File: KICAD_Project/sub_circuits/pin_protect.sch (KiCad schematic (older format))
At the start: 84 parts

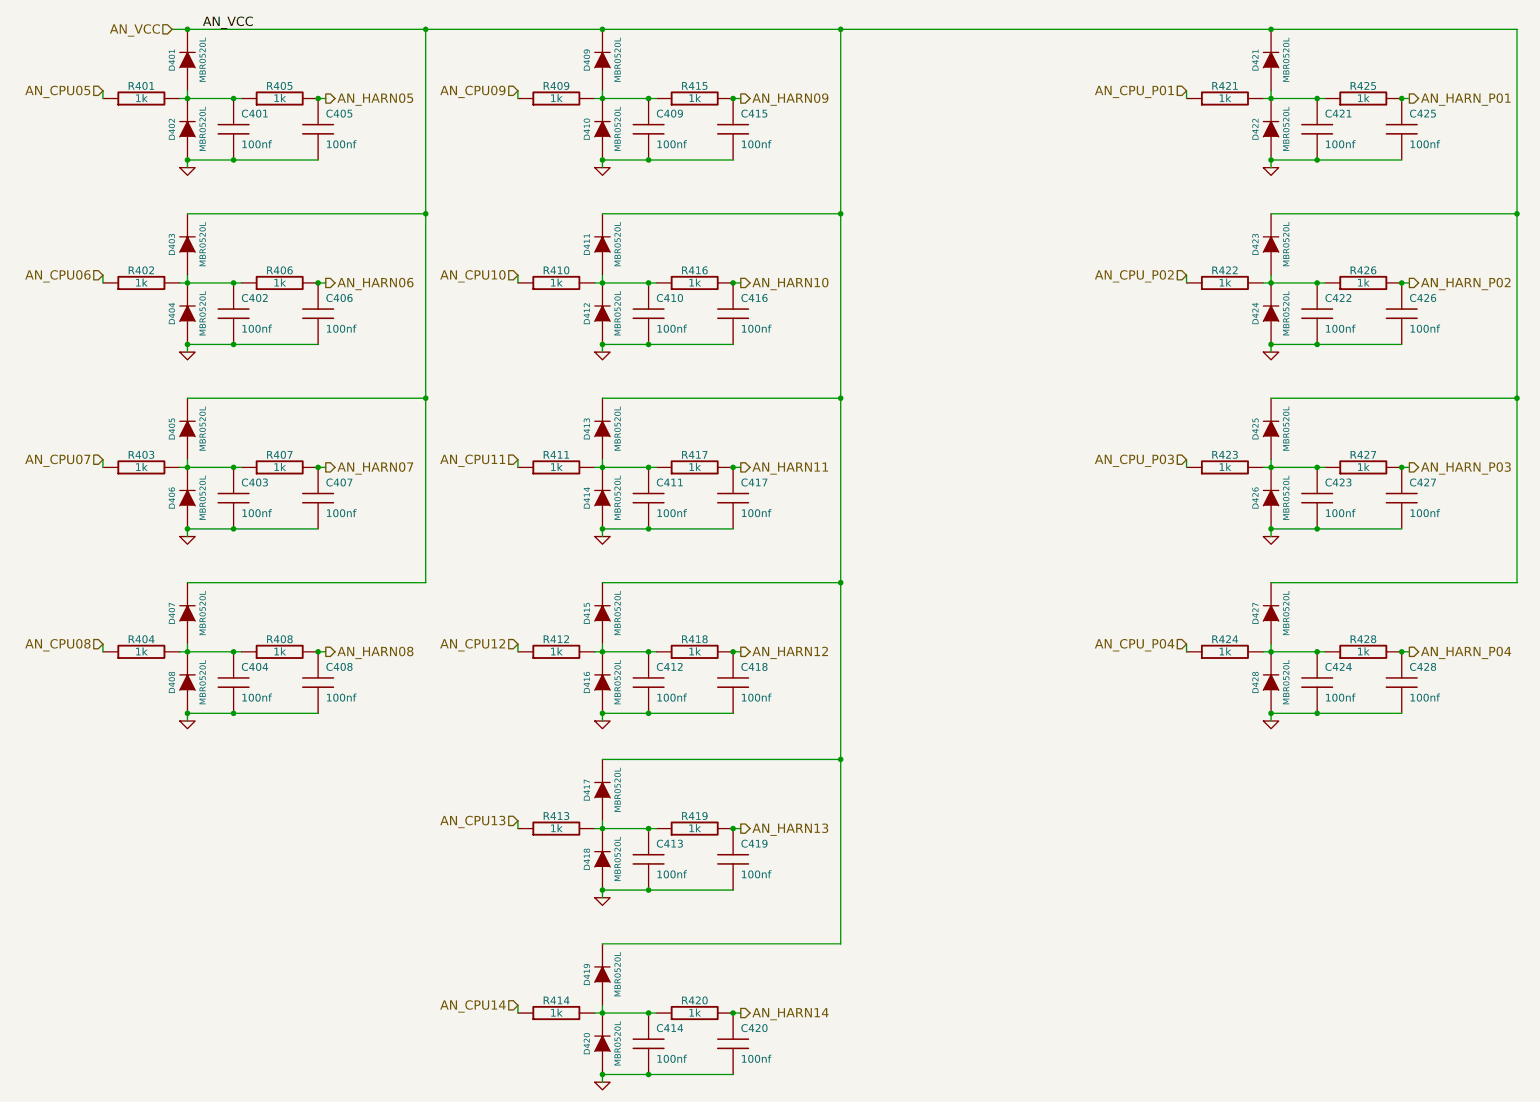
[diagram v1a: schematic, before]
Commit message: Added some simulations for the AN protect lines
Signed-off-by: Jared Harvey <TortiseGIT@jaredharvey.com>
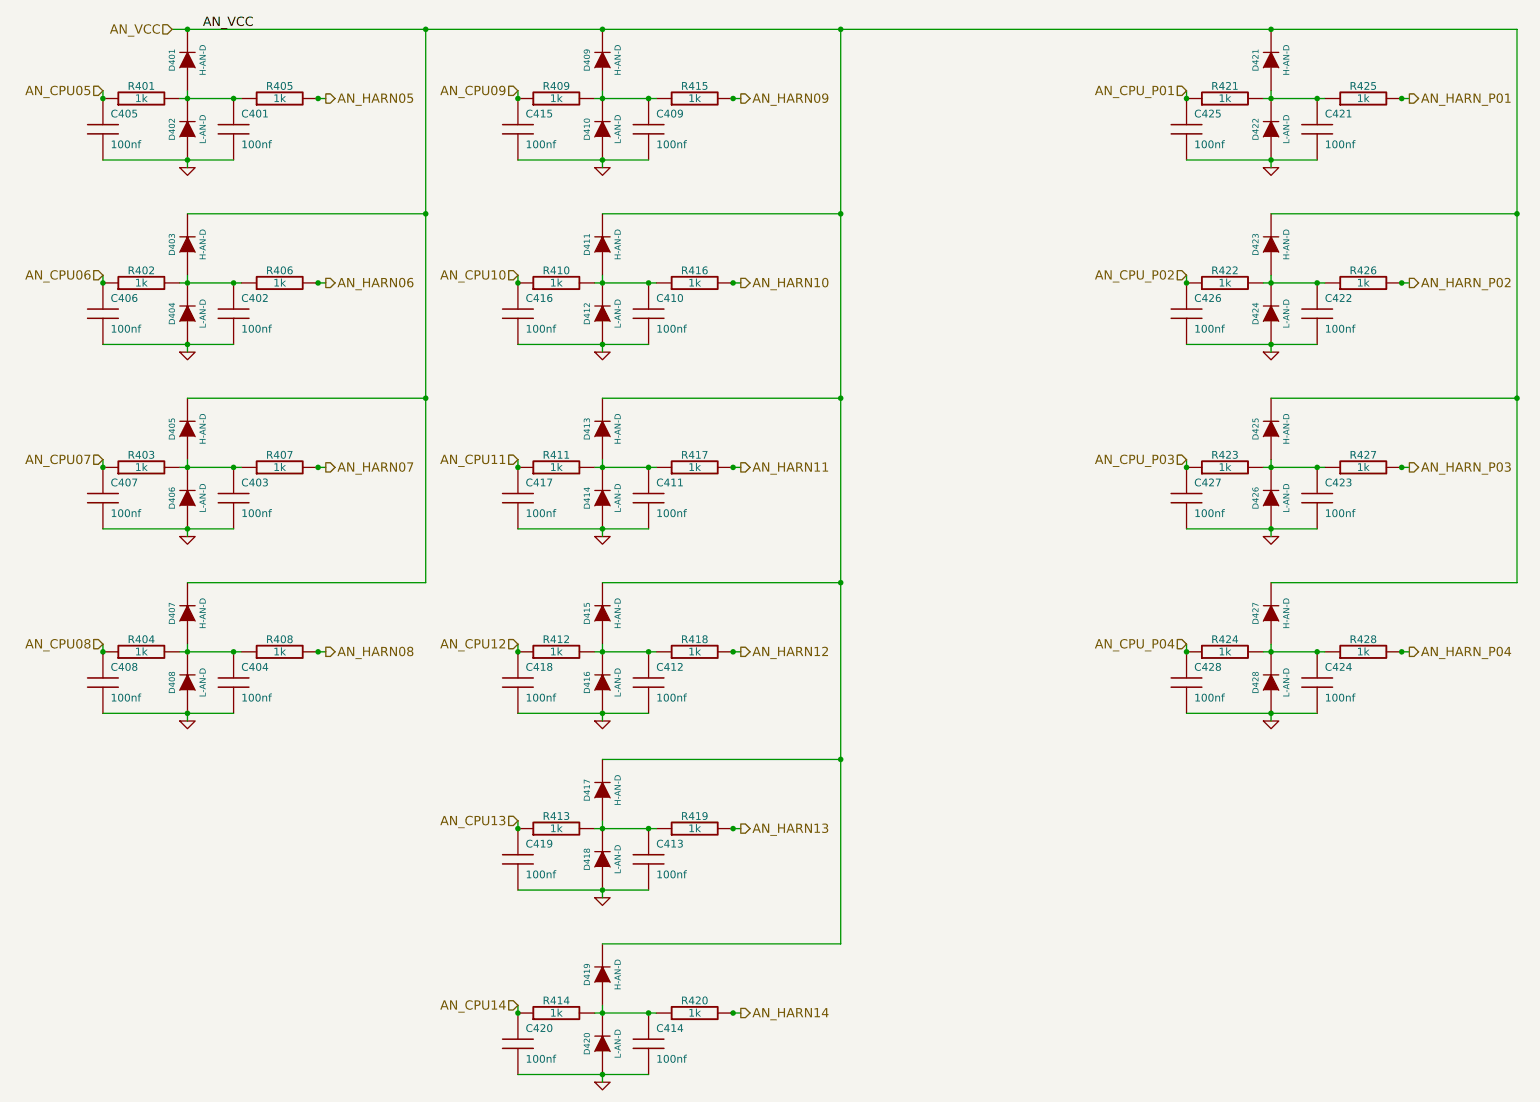
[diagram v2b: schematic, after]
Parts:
- D401, D403, D405, D407, D409, D411, D413, D415, D417, D419, D421, D423, D425, D427: value MBR0520L -> H-AN-D
- D402, D404, D406, D408, D410, D412, D414, D416, D418, D420, D422, D424, D426, D428: value MBR0520L -> L-AN-D
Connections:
- net AN_CPU05: now also C405.1
- net AN_CPU06: now also C406.1
- net AN_CPU07: now also C407.1
- net AN_CPU08: now also C408.1
- net AN_CPU09: now also C415.1
- net AN_CPU10: now also C416.1
- net AN_CPU11: now also C417.1
- net AN_CPU12: now also C418.1
- net AN_CPU13: now also C419.1
- net AN_CPU14: now also C420.1
- net AN_CPU_P01: now also C425.1
- net AN_CPU_P02: now also C426.1
- net AN_CPU_P03: now also C427.1
- net AN_CPU_P04: now also C428.1
- net AN_HARN05: no longer C405.1
- net AN_HARN06: no longer C406.1
- net AN_HARN07: no longer C407.1
- net AN_HARN08: no longer C408.1
- net AN_HARN09: no longer C415.1
- net AN_HARN10: no longer C416.1
- net AN_HARN11: no longer C417.1
- net AN_HARN12: no longer C418.1
- net AN_HARN13: no longer C419.1
- net AN_HARN14: no longer C420.1
- net AN_HARN_P01: no longer C425.1
- net AN_HARN_P02: no longer C426.1
- net AN_HARN_P03: no longer C427.1
- net AN_HARN_P04: no longer C428.1
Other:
- moved on the sheet: C405, C406, C407, C408, C415, C416, C417, C418, C419, C420, C425, C426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

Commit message: Did a bit more layout work.
Signed-off-by: Jared Harvey <TortiseGIT@jaredharvey.com>
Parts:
- added U401: SP720, SO16E, symbol SP720
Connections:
- net labels added: 12V_BAT
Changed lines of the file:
@@
-EESchema Schematic File Version 2  date 10/4/2011 8:27:03 PM
+EESchema Schematic File Version 2  date 10/11/2011 7:34:29 AM
 LIBS:power
 LIBS:device
@@
 encoding utf-8
 Sheet 4 12
-Title "freeEMS PLUS from Cinch template "
-Date "5 oct 2011"
+Title "Open5xxxECU (o5e), an ECU that is no longer affiliated with freeEMS."
+Date "11 oct 2011"
 Rev "A-DRAFT5"
-Comp "diyefi.org/openecu.info"
+Comp "http://open5xxxecu.org/"
 Comment1 "misc analog input protection circuits"
 Comment2 ""
@@
 Comment4 ""
 $EndDescr
+Text HLabel 7800 6450 0    60   Output ~ 0
+AN_HARN11
+Text HLabel 7800 6350 0    60   Output ~ 0
+AN_HARN10
+Text HLabel 7800 6250 0    60   Output ~ 0
+AN_HARN09
+Text HLabel 7800 6150 0    60   Output ~ 0
+AN_HARN08
+Text HLabel 7800 6050 0    60   Output ~ 0
+AN_HARN07
+Text HLabel 7800 5950 0    60   Output ~ 0
+AN_HARN06
+Text HLabel 7800 5850 0    60   Output ~ 0
+AN_HARN05
+Text HLabel 8900 6550 2    60   Output ~ 0
+AN_HARN12
+Text HLabel 8900 6450 2    60   Output ~ 0
+AN_HARN13
+Text HLabel 8900 6350 2    60   Output ~ 0
+AN_HARN14
+Text HLabel 8900 6250 2    60   Output ~ 0
+AN_HARN_P04
+Text HLabel 8900 6150 2    60   Output ~ 0
+AN_HARN_P03
+Text HLabel 8900 6050 2    60   Output ~ 0
+AN_HARN_P02
+Text HLabel 8900 5950 2    60   Output ~ 0
+AN_HARN_P01
+Text HLabel 8900 5850 2    60   Input ~ 0
+12V_BAT
+$Comp
+L GND #PWR086
+U 1 1 4E9423F6
+P 7800 6550
+F 0 "#PWR086" H 7800 6550 30  0001 C CNN
+F 1 "GND" H 7800 6480 30  0001 C CNN
+	1    7800 6550
+	1    0    0    -1
+$EndComp
+$Comp
+L SP720 U401
+U 1 1 4E9423E8
+P 8350 6200
+F 0 "U401" H 8350 6700 60  0000 C CNN
+F 1 "SP720" H 8350 5700 60  0000 C CNN
+F 2 "SO16E" H 8350 6000 60  0001 C CNN
+	1    8350 6200
+	1    0    0    -1
+$EndComp
 Wire Wire Line
 	3750 1500 4600 1500
@@
 $EndComp
 $Comp
-L GND #PWR086
+L GND #PWR087
 U 1 1 4E4DAF8E
 P 4300 6300
-F 0 "#PWR086" H 4300 6300 30  0001 C CNN
+F 0 "#PWR087" H 4300 6300 30  0001 C CNN
 F 1 "GND" H 4300 6230 30  0001 C CNN
 	1    4300 6300
@@
 $EndComp
 $Comp
-L GND #PWR087
+L GND #PWR088
 U 1 1 4E4DAF87
 P 4300 7500
-F 0 "#PWR087" H 4300 7500 30  0001 C CNN
+F 0 "#PWR088" H 4300 7500 30  0001 C CNN
 F 1 "GND" H 4300 7430 30  0001 C CNN
 	1    4300 7500
@@
 $EndComp
 $Comp
-L GND #PWR088
+L GND #PWR089
 U 1 1 4E4DACB4
 P 8650 5150
-F 0 "#PWR088" H 8650 5150 30  0001 C CNN
+F 0 "#PWR089" H 8650 5150 30  0001 C CNN
 F 1 "GND" H 8650 5080 30  0001 C CNN
 	1    8650 5150
@@
 $EndComp
 $Comp
-L GND #PWR089
+L GND #PWR090
 U 1 1 4E47D7F8
 P 8650 3950
-F 0 "#PWR089" H 8650 3950 30  0001 C CNN
+F 0 "#PWR090" H 8650 3950 30  0001 C CNN
 F 1 "GND" H 8650 3880 30  0001 C CNN
 	1    8650 3950
@@
 $EndComp
 $Comp
-L GND #PWR090
+L GND #PWR091
 U 1 1 4E47D7F1
 P 8650 2750
-F 0 "#PWR090" H 8650 2750 30  0001 C CNN
+F 0 "#PWR091" H 8650 2750 30  0001 C CNN
 F 1 "GND" H 8650 2680 30  0001 C CNN
 	1    8650 2750
@@
 $EndComp
 $Comp
-L GND #PWR091
+L GND #PWR092
 U 1 1 4E47D7E6
 P 8650 1550
-F 0 "#PWR091" H 8650 1550 30  0001 C CNN
+F 0 "#PWR092" H 8650 1550 30  0001 C CNN
 F 1 "GND" H 8650 1480 30  0001 C CNN
 	1    8650 1550
@@
 $EndComp
 $Comp
-L GND #PWR092
+L GND #PWR093
 U 1 1 4E47D7E3
 P 4300 1550
-F 0 "#PWR092" H 4300 1550 30  0001 C CNN
+F 0 "#PWR093" H 4300 1550 30  0001 C CNN
 F 1 "GND" H 4300 1480 30  0001 C CNN
 	1    4300 1550
@@
 $EndComp
 $Comp
-L GND #PWR093
+L GND #PWR094
 U 1 1 4E47D7D8
 P 4300 2750
-F 0 "#PWR093" H 4300 2750 30  0001 C CNN
+F 0 "#PWR094" H 4300 2750 30  0001 C CNN
 F 1 "GND" H 4300 2680 30  0001 C CNN
 	1    4300 2750
@@
 $EndComp
 $Comp
-L GND #PWR094
+L GND #PWR095
 U 1 1 4E47D7D5
 P 4300 5150
-F 0 "#PWR094" H 4300 5150 30  0001 C CNN
+F 0 "#PWR095" H 4300 5150 30  0001 C CNN
 F 1 "GND" H 4300 5080 30  0001 C CNN
 	1    4300 5150
@@
 $EndComp
 $Comp
-L GND #PWR095
+L GND #PWR096
 U 1 1 4E47D7CA
 P 4300 3950
-F 0 "#PWR095" H 4300 3950 30  0001 C CNN
+F 0 "#PWR096" H 4300 3950 30  0001 C CNN
 F 1 "GND" H 4300 3880 30  0001 C CNN
 	1    4300 3950
@@
 $EndComp
 $Comp
-L GND #PWR096
+L GND #PWR097
 U 1 1 4E47D792
 P 1600 3950
-F 0 "#PWR096" H 1600 3950 30  0001 C CNN
+F 0 "#PWR097" H 1600 3950 30  0001 C CNN
 F 1 "GND" H 1600 3880 30  0001 C CNN
 	1    1600 3950
@@
 $EndComp
 $Comp
-L GND #PWR097
+L GND #PWR098
 U 1 1 4E47D787
 P 1600 5150
-F 0 "#PWR097" H 1600 5150 30  0001 C CNN
+F 0 "#PWR098" H 1600 5150 30  0001 C CNN
 F 1 "GND" H 1600 5080 30  0001 C CNN
 	1    1600 5150
@@
 $EndComp
 $Comp
-L GND #PWR098
+L GND #PWR099
 U 1 1 4E47D767
 P 1600 2750
-F 0 "#PWR098" H 1600 2750 30  0001 C CNN
+F 0 "#PWR099" H 1600 2750 30  0001 C CNN
 F 1 "GND" H 1600 2680 30  0001 C CNN
 	1    1600 2750
@@
 $EndComp
 $Comp
-L GND #PWR099
+L GND #PWR0100
 U 1 1 4E47D48E
 P 1600 1550
-F 0 "#PWR099" H 1600 1550 30  0001 C CNN
+F 0 "#PWR0100" H 1600 1550 30  0001 C CNN
 F 1 "GND" H 1600 1480 30  0001 C CNN
 	1    1600 1550

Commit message: Changed AN protections to match QUCS simulation predictions.
Signed-off-by: Jared Harvey <TortiseGIT@jaredharvey.com>
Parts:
- removed C401, C402, C403, C404, C409, C410, C411, C412, C413, C414, C421, C422, C423, C424: 100nf, SM0805-C1, symbol C
- removed R401, R402, R403, R404, R409, R410, R411, R412, R413, R414, R421, R422, R423, R424: 1k, SM0805, symbol R
- C405, C406, C407, C408, C415, C416, C417, C418, C419, C420, C425, C426, C427, C428: value 100nf -> .01uf
- R405, R406, R407, R408, R415, R416, R417, R418, R419, R420, R425, R426, R427, R428: value 1k -> 2.2k

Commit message: Made more progress on the AN protects and LS drive 33800
Signed-off-by: Jared Harvey <TortiseGIT@jaredharvey.com>
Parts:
- C405, C406, C407, C408, C415, C416, C417, C418, C419, C420, C425, C426, C427, C428: footprint SM0805-C1 -> SM0805; % (none) -> 10%; V 100V -> 50V; mfg,mfg# avx,08051C104KAT2A -> avx,08055C103KAT2A; tolerance 10% -> (none); vend1,vend1# newark,96M1354 -> newark,07J3575
- D401, D402, D403, D404, D405, D406, D407, D408, D409, D410, D411, D412, D413, D414, D415, D416, D417, D418, D419, D420, D421, D422, D423, D424, D425, D426, D427, D428: Field3 -,- -> (none); Field4 -,- -> (none); Field5 20,V-reverse -> (none); Field6 .5,A-forward -> (none); Field7 SMT -> (none); Field8 other,more,stuff -> (none); construct (none) -> schottky; forward A (none) -> 200mA; mfg,# fairchild,MBR0520L -> (none); mfg,mfg# (none) -> ON-SEMI,BAT54T1G; misc (none) -> other,more,stuff; reverse V (none) -> 30V; vend,# mouser,512-MBR0520L -> (none); vend1,vend1# (none) -> NEWARK,67R1284
- R405, R406, R407, R408, R415, R416, R417, R418, R419, R420, R425, R426, R427, R428: % (none) -> 1%; TOL 1% -> (none); W 125mW -> .125W; construct THICK FILM -> thick film; mfg,mfg# vishay,CRCW08051K00FKTA -> vishay,CRCW08052K21FKEA; vend1,vend1# newark,05F1507 -> newark,52K9952
